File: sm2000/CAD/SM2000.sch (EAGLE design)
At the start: 398 parts, among them CN1 HDR100-3, CN2 ST-3509, CN3 HDR100-3, CN4 JS-MU3-002, CN5 DS-0518, CN6 ST-3509, CN7 ST-3509, J1 JMP-2PIN, J10 JMPR-2X2, J11 JMPR-2X2, J12 JMPR-2X2, J13 JMPR-2X2, J14 JMPR-2X2, J2 HDR100-7, J3 JMP-2PIN, J4 CONN-BOOM-XH-2A, J5 JMP-2PIN, J6 JMPR-2X2, J7 JMPR-2X2, J8 JMPR-2X2, J9 JMPR-2X2, P6 TPAD50, P7 TPAD50, P8 TPAD50, P9 TPAD50, Q1 MMBT3904, Q10 MMBT3904, Q11 BFR92, Q12 BFQ19, Q13 RD01MUS2, Q14 MMBT3904, Q15 MMBT3904, Q16 MMBT3904, Q17 MMBT3906, Q2 STR2P3LLH6, Q3 MMBT3904, Q4 STR2P3LLH6, Q5 MMBT3904, Q6 MMBT3904, Q7 MMBT3904, Q8 MMBT3904, Q9 MMBT3904, SW1 TS-02B, SW2 SW-LC2259, SW3 TS-026, SW4 TS-026, SW5 SW-LC2259EENP, U1 STM32F405VGT6, U10 LM386M-1, U11 ADE-1, U12 PGA-103+, U13 LMV341, U14 SI5351A, U15 SI570, U16 SA612A, U2 STMPS2141, U3 EMIF02-USB03F2, U4 DNL, U5 L78M09, U6 LD1117AS-33, U7 LMV341, U8 LD1117AS-33, U9 TPS54329E, X1 BU-SMA-H

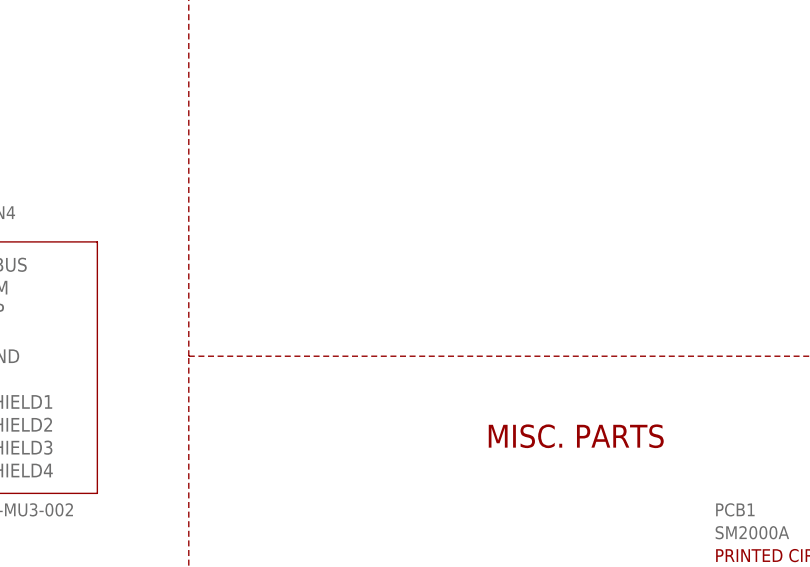
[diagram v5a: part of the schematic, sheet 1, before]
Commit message: Added Shield mounting tabs(7) to schematic & PCB. Moved, rotated and restructured RF blocks on PCB in proparation for routing. RGB
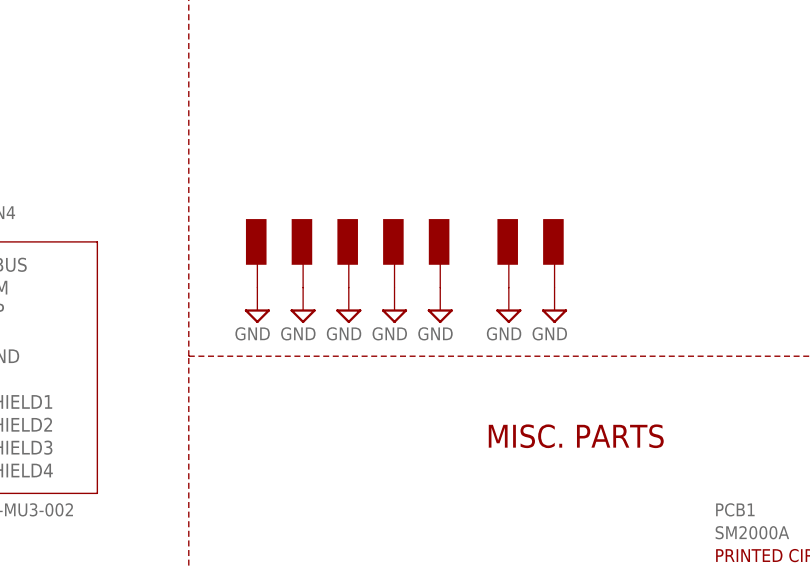
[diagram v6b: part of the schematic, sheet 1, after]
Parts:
- added S1, S2, S3, S4, S5, S6, S7: SGND, _RoweTel:SGND
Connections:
- net GND: now also S1.P$1, S2.P$1, S3.P$1, S4.P$1, S5.P$1, S6.P$1, S7.P$1
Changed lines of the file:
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@@
 <class number="0" name="default" width="0" drill="0">
+</class>
+<class number="1" name="Stripline" width="0.508" drill="0.508">
+<clearance class="1" value="0.508"/>
 </class>
 </classes>
@@
 <part name="XTAL2" library="_RoweTel" deviceset="CTS-405" device="" value="25.000MHz"/>
 <part name="C83" library="_RoweTel" deviceset="TRIMCAP_VAR_2222_V" device="" value="2-12pF"/>
+<part name="S1" library="_RoweTel" deviceset="SGND" device=""/>
+<part name="S2" library="_RoweTel" deviceset="SGND" device=""/>
+<part name="S3" library="_RoweTel" deviceset="SGND" device=""/>
+<part name="S4" library="_RoweTel" deviceset="SGND" device=""/>
+<part name="S5" library="_RoweTel" deviceset="SGND" device=""/>
+<part name="S6" library="_RoweTel" deviceset="SGND" device=""/>
+<part name="S7" library="_RoweTel" deviceset="SGND" device=""/>
+<part name="V90" library="A-SUPPLY2" deviceset="GND" device=""/>
+<part name="V111" library="A-SUPPLY2" deviceset="GND" device=""/>
+<part name="V116" library="A-SUPPLY2" deviceset="GND" device=""/>
+<part name="V117" library="A-SUPPLY2" deviceset="GND" device=""/>
+<part name="V123" library="A-SUPPLY2" deviceset="GND" device=""/>
+<part name="V138" library="A-SUPPLY2" deviceset="GND" device=""/>
+<part name="V139" library="A-SUPPLY2" deviceset="GND" device=""/>
 </parts>
 <sheets>
@@
 </instance>
 <instance part="XTAL1" gate="G$1" x="236.22" y="193.04"/>
+<instance part="S1" gate="G$1" x="337.82" y="83.82"/>
+<instance part="S2" gate="G$1" x="342.9" y="83.82"/>
+<instance part="S3" gate="G$1" x="347.98" y="83.82"/>
+<instance part="S4" gate="G$1" x="353.06" y="83.82"/>
+<instance part="S5" gate="G$1" x="358.14" y="83.82"/>
+<instance part="S6" gate="G$1" x="365.76" y="83.82"/>
+<instance part="S7" gate="G$1" x="370.84" y="83.82"/>
+<instance part="V90" gate="GND" x="337.82" y="76.2"/>
+<instance part="V111" gate="GND" x="342.9" y="76.2"/>
+<instance part="V116" gate="GND" x="347.98" y="76.2"/>
+<instance part="V117" gate="GND" x="353.06" y="76.2"/>
+<instance part="V123" gate="GND" x="358.14" y="76.2"/>
+<instance part="V138" gate="GND" x="365.76" y="76.2"/>
+<instance part="V139" gate="GND" x="370.84" y="76.2"/>
 </instances>
 <busses>
@@
 <wire x1="223.52" y1="190.5" x2="223.52" y2="180.34" width="0.1524" layer="91"/>
 </segment>
+<segment>
+<pinref part="S1" gate="G$1" pin="P$1"/>
+<pinref part="V90" gate="GND" pin="GND"/>
+</segment>
+<segment>
+<pinref part="S2" gate="G$1" pin="P$1"/>
+<pinref part="V111" gate="GND" pin="GND"/>
+</segment>
+<segment>
+<pinref part="S3" gate="G$1" pin="P$1"/>
+<pinref part="V116" gate="GND" pin="GND"/>
+</segment>
+<segment>
+<pinref part="S4" gate="G$1" pin="P$1"/>
+<pinref part="V117" gate="GND" pin="GND"/>
+</segment>
+<segment>
+<pinref part="S5" gate="G$1" pin="P$1"/>
+<pinref part="V123" gate="GND" pin="GND"/>
+</segment>
+<segment>
+<pinref part="S6" gate="G$1" pin="P$1"/>
+<pinref part="V138" gate="GND" pin="GND"/>
+</segment>
+<segment>
+<pinref part="S7" gate="G$1" pin="P$1"/>
+<pinref part="V139" gate="GND" pin="GND"/>
+</segment>
 </net>

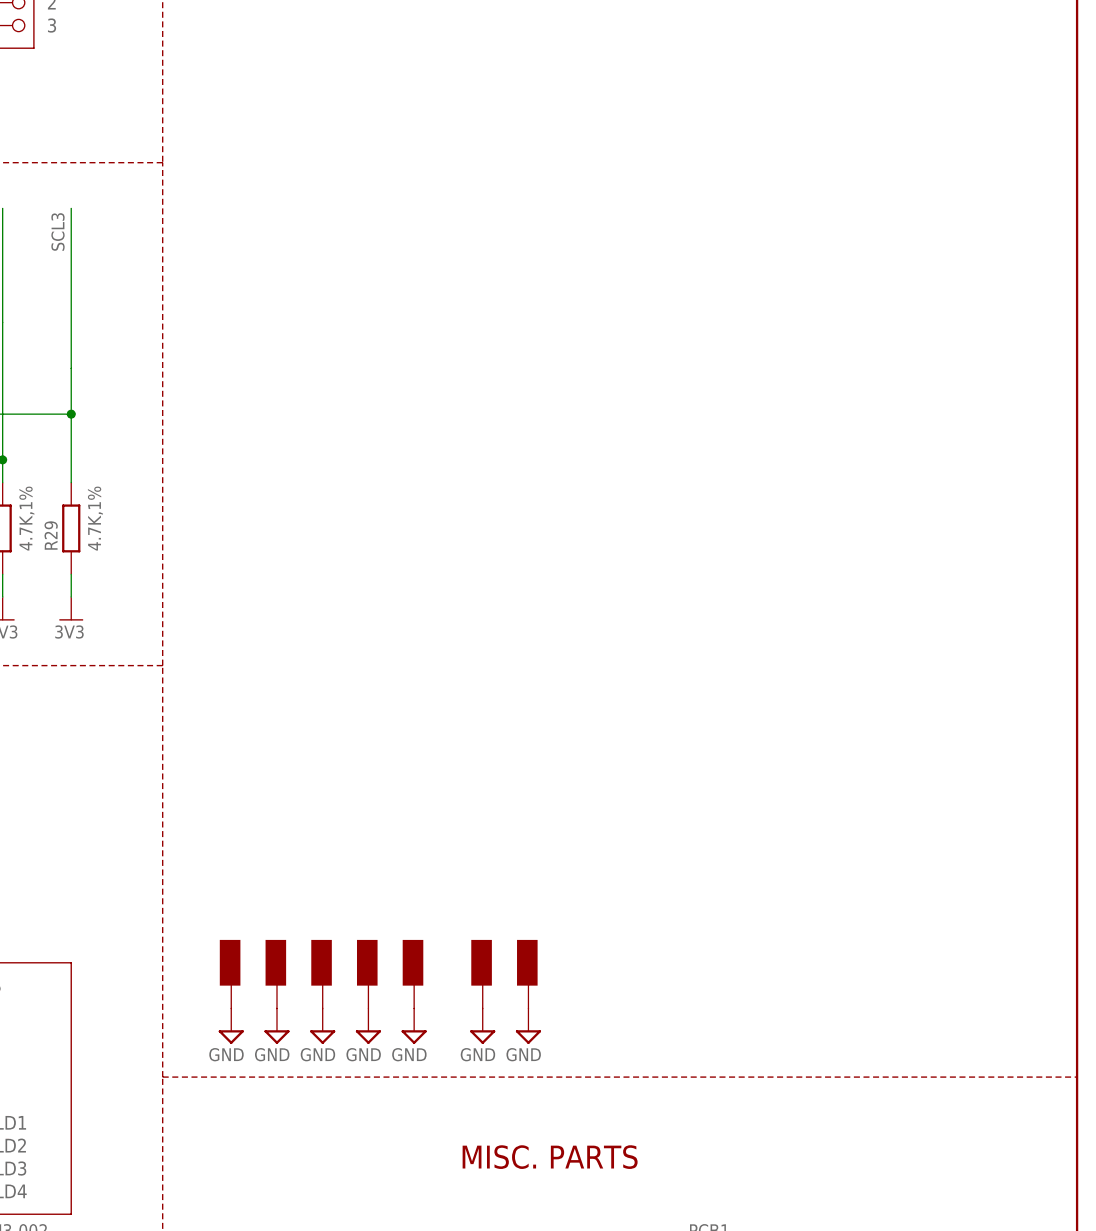
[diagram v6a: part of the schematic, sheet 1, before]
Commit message: Current status as of 4/4/16 RGB
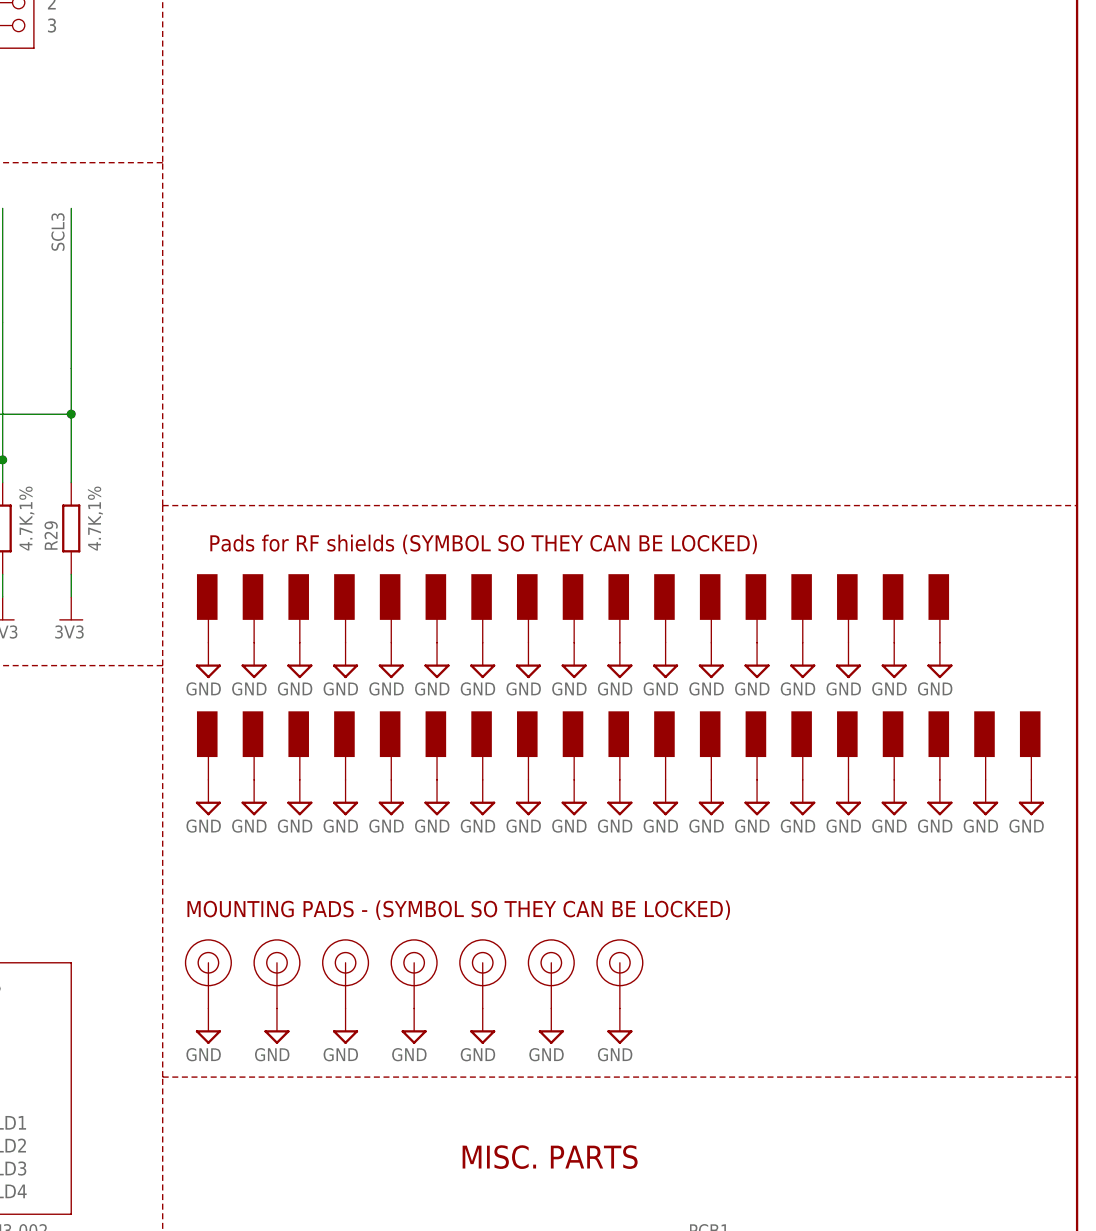
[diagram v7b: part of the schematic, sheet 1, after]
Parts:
- added PAD1, PAD2, PAD3, PAD4, PAD5, PAD6, PAD7: MTG-PAD-3.2, _RoweTel:MTG-PAD-3.2
- added S10, S11, S12, S13, S14, S15, S16, S17, S18, S19, S20, S21, S22, S23, S24, S25, S26, S27, S28, S29, S30, S31, S32, S33, S34, S35, S36, S8, S9: SGND, _RoweTel:SGND
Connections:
- net GND: now also PAD1.P$1, PAD2.P$1, PAD3.P$1, PAD4.P$1, PAD5.P$1, PAD6.P$1, PAD7.P$1, S1.1, S10.1, S11.1, S12.1, S13.1, S14.1, S15.1, S16.1, S17.1, S18.1, S19.1, S2.1, S20.1, S21.1, S22.1, S23.1, S24.1, S25.1, S26.1, S27.1, S28.1, S29.1, S3.1, S30.1, S31.1, S32.1, S33.1, S34.1, S35.1, S36.1, S4.1, S5.1, S6.1, S7.1, S8.1, S9.1; no longer S1.P$1, S2.P$1, S3.P$1, S4.P$1, S5.P$1, S6.P$1, S7.P$1
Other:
- note added: "MOUNTING PADS - (SYMBOL SO THEY CAN BE LOCKED)"
- note added: "Pads for RF shields (SYMBOL SO THEY CAN BE LOCKED)"

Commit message: LAYOUT UPDATES as of 4/13/16  RGB 80 NODES to COMPLETE
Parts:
- added S37, S38, S39, S40, S41, S42, S43: SGND, _RoweTel:SGND
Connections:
- net GND: now also S37.1, S38.1, S39.1, S40.1, S41.1, S42.1, S43.1
